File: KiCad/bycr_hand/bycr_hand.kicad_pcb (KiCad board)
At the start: 2 copper layers, 26 parts, among them J1 Conn_01x03, J2 Conn_01x03, J3 Conn_01x03, J4 Conn_01x03, J5 Conn_01x02, J6 Conn_01x02, SW1 SW_Push, U1 74HC595, U3 74HC165

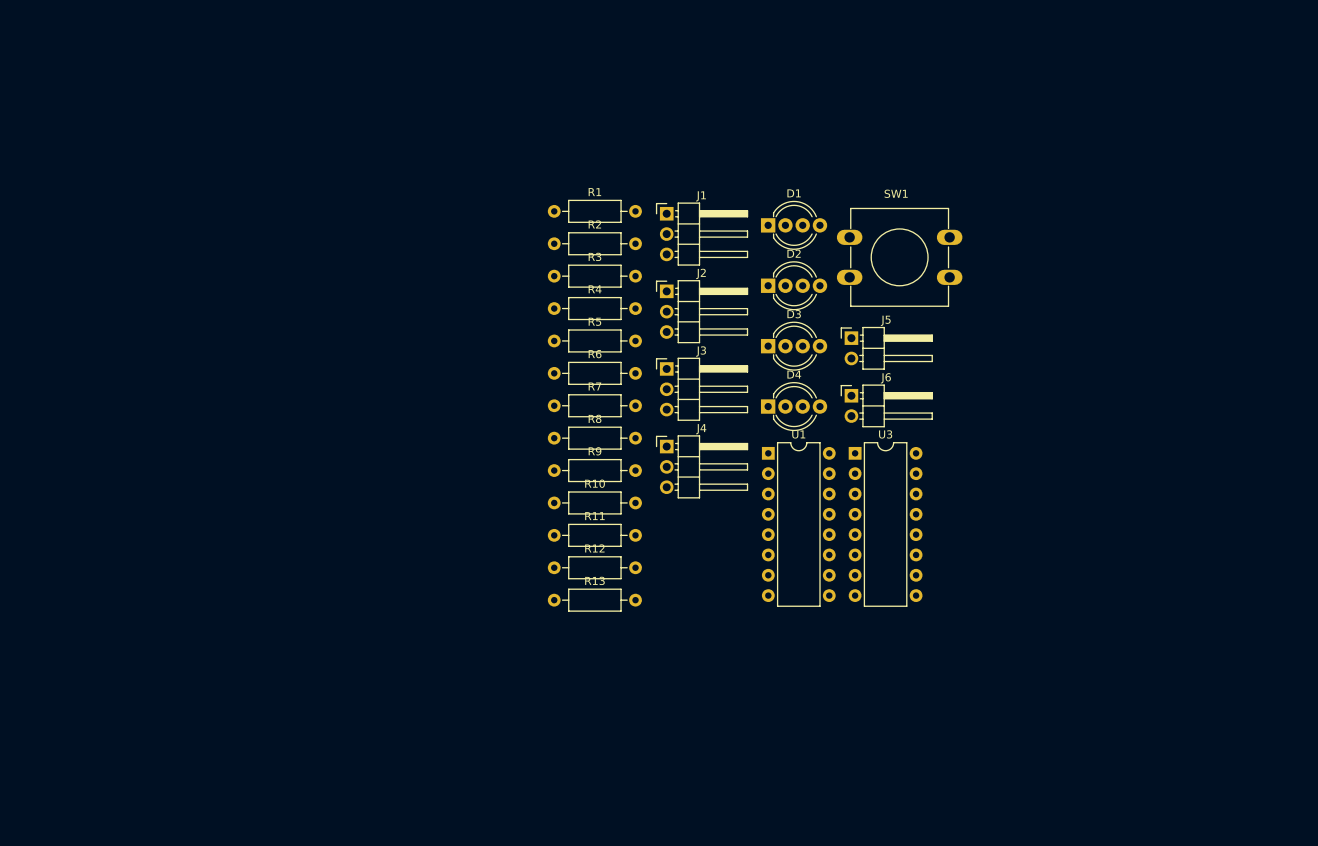
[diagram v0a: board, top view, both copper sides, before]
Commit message: rename bycr to bycr_hand
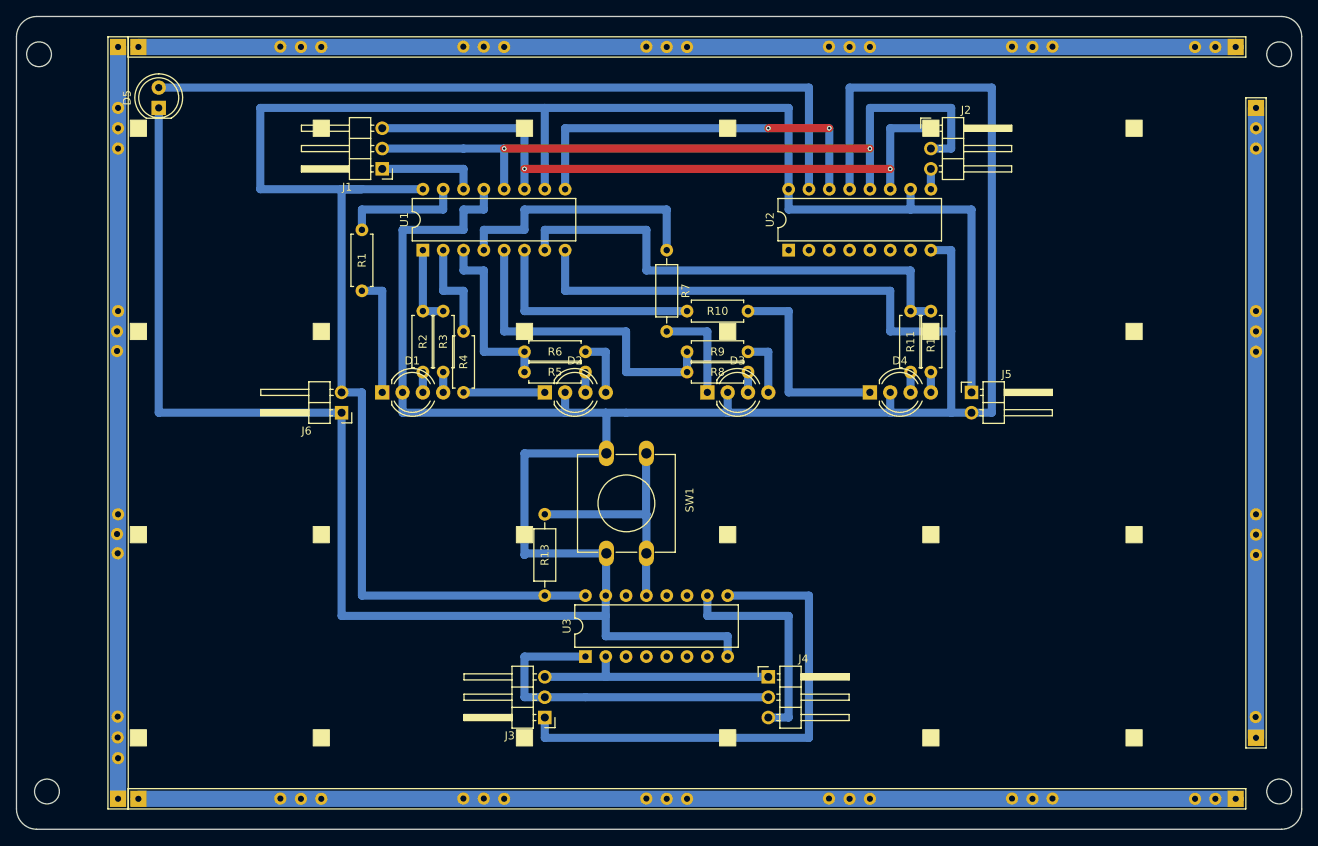
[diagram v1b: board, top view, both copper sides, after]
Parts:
- added D5: LED, LED_THT:LED_D5.0mm, F.Cu at (86.4, 58.4)
- added REF**: PCB_M, New_Library:PCB_M, F.Cu at (81.3, 50.8)
- added U2: 74HC595, Package_DIP:DIP-16_W7.62mm, F.Cu at (165.1, 76.2)
- D1, D2, D3, D4: footprint LED_THT:LED_D5.0mm-4_RGB_Wide_Pins -> Custom:LED_D5.0mm-4_RGB_Wide_Pins_Custom
- R1, R10, R11, R12, R2, R3, R4, R5, R6, R8, R9: footprint Resistor_THT:R_Axial_DIN0207_L6.3mm_D2.5mm_P10.16mm_Horizontal -> Resistor_THT:R_Axial_DIN0207_L6.3mm_D2.5mm_P7.62mm_Horizontal
- moved J6 63.8 mm to (109.2, 96.5), turned to 180 degrees
- moved R12 57.0 mm to (182.9, 83.8), turned to -90 degrees
- moved R11 52.6 mm to (180.3, 83.8), turned to -90 degrees
- moved D1 52.1 mm to (114.8, 94.0)
- moved U1 50.1 mm to (119.4, 76.2), turned to 90 degrees
- moved J3 46.2 mm to (134.6, 134.6), turned to 180 degrees
- moved U3 42.2 mm to (139.7, 127.0), turned to 90 degrees
- moved J2 38.8 mm to (182.9, 61.0)
- moved SW1 37.1 mm to (147.3, 101.6), turned to -90 degrees
- moved J1 36.0 mm to (114.3, 66.0), turned to 180 degrees
- moved J4 31.5 mm to (162.6, 129.5)
- moved D2 30.5 mm to (135.1, 94.0)
- moved R10 29.2 mm to (152.4, 83.8)
- moved R1 24.2 mm to (111.8, 73.7), turned to -90 degrees
- moved R7 24.0 mm to (149.9, 76.2), turned to -90 degrees
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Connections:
- J2 pad 1: Net-(J2-Pin_1) -> /output_clk
- J2 pad 3: /output_clk -> Net-(J2-Pin_3)
- J4 pad 1: Net-(J4-Pin_1) -> /input_clk
- J4 pad 3: /input_clk -> Net-(J4-Pin_3)
- J5 pad 1: GNDREF -> VCC
- J5 pad 2: VCC -> GNDREF
- R13 pad 2: Net-(U3-D7) -> Net-(U3-D2)
- SW1 pad 1: Net-(U3-D7) -> Net-(U3-D2)
- U1 pad 11: /output_latch -> /output_clk
- U1 pad 12: /output_clk -> /output_latch
- U1 pad 9: Net-(J2-Pin_1) -> Net-(U1-QH')
- U3 pad 10: Net-(J4-Pin_1) -> Net-(J4-Pin_3)
- U3 pad 13: unconnected-(U3-D2-Pad13) -> Net-(U3-D2)
- U3 pad 6: Net-(U3-D7) -> unconnected-(U3-D7-Pad6)
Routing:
- net GNDREF: track 0.00 -> 457.7 mm
- net VCC: track 0.00 -> 254.0 mm
- net Net-(D5-A): track 0.00 -> 94.0 mm
- net /output_latch: track 0.00 -> 94.0 mm, vias 0 -> 2
- net /output_clk: track 0.00 -> 83.8 mm, vias 0 -> 2
- net Net-(J3-Pin_1): track 0.00 -> 63.5 mm
- net Net-(U1-QH): track 0.00 -> 61.0 mm
- net Net-(U1-QH'): track 0.00 -> 48.3 mm, vias 0 -> 2
- net /input_latch: track 0.00 -> 43.2 mm
- net Net-(U1-QF): track 0.00 -> 40.6 mm
- net Net-(U1-QE): track 0.00 -> 33.0 mm
- net /input_clk: track 0.00 -> 30.5 mm
- net Net-(U3-D2): track 0.00 -> 29.2 mm
- net Net-(J4-Pin_3): track 0.00 -> 27.9 mm
- net Net-(U1-QG): track 0.00 -> 27.9 mm
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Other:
- board outline added: 160.7 x 101.6 mm

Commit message: fix bycr PCB layout
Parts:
- moved D1 2.54 mm to (112.3, 94.0)
- moved R3 2.54 mm to (119.4, 83.8)
- moved R2 2.54 mm to (116.8, 83.8)
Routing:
- net VCC: track 254.0 -> 236.2 mm
- net GNDREF: track 457.7 -> 447.5 mm
- net Net-(D1-RA): track 15.2 -> 12.7 mm
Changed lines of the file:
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@@
 	(footprint "Custom:LED_D5.0mm-4_RGB_Wide_Pins_Custom"
 		(layer "F.Cu")
-		(at 114.808 93.98)
+		(at 112.268 93.98)
 		(descr "LED, diameter 5.0mm, 4 pins, WP154A4, https://www.kingbright.com/attachments/file/psearch/000/00/00/L-154A4SUREQBFZGEW(Ver.11A).pdf")
 		(tags "LED diameter 5.0mm 2 pins diameter 5.0mm 3 pins diameter 5.0mm 4 pins RGB RGBLED")
@@
 	(footprint "Resistor_THT:R_Axial_DIN0207_L6.3mm_D2.5mm_P7.62mm_Horizontal"
 		(layer "F.Cu")
-		(at 121.92 83.82 -90)
+		(at 119.38 83.82 -90)
 		(descr "Resistor, Axial_DIN0207 series, Axial, Horizontal, pin pitch=7.62mm, 0.25W = 1/4W, length*diameter=6.3*2.5mm^2, http://cdn-reichelt.de/documents/datenblatt/B400/1_4W%23YAG.pdf")
 		(tags "Resistor Axial_DIN0207 series Axial Horizontal pin pitch 7.62mm 0.25W = 1/4W length 6.3mm diameter 2.5mm")
@@
 	(footprint "Resistor_THT:R_Axial_DIN0207_L6.3mm_D2.5mm_P7.62mm_Horizontal"
 		(layer "F.Cu")
-		(at 119.38 83.82 -90)
+		(at 116.84 83.82 -90)
 		(descr "Resistor, Axial_DIN0207 series, Axial, Horizontal, pin pitch=7.62mm, 0.25W = 1/4W, length*diameter=6.3*2.5mm^2, http://cdn-reichelt.de/documents/datenblatt/B400/1_4W%23YAG.pdf")
 		(tags "Resistor Axial_DIN0207 series Axial Horizontal pin pitch 7.62mm 0.25W = 1/4W length 6.3mm diameter 2.5mm")
@@
 	)
 	(segment
-		(start 114.3 81.28)
-		(end 114.3 93.98)
+		(start 111.76 81.28)
+		(end 111.76 93.98)
 		(width 1.016)
 		(layer "B.Cu")
@@
 	)
 	(segment
-		(start 111.76 81.28)
-		(end 114.3 81.28)
+		(start 119.38 91.44)
+		(end 119.38 93.98)
 		(width 1.016)
 		(layer "B.Cu")
-		(net 1)
+		(net 2)
 	)
 	(segment
-		(start 121.92 91.44)
-		(end 121.92 93.599)
+		(start 116.84 91.44)
+		(end 116.84 93.98)
 		(width 1.016)
 		(layer "B.Cu")
-		(net 2)
+		(net 3)
 	)
 	(segment
-		(start 121.92 93.599)
-		(end 121.539 93.98)
+		(start 114.3 93.98)
+		(end 114.3 96.52)
 		(width 1.016)
 		(layer "B.Cu")
-		(net 2)
+		(net 4)
 	)
 	(segment
-		(start 119.38 91.44)
-		(end 119.38 93.98)
+		(start 114.3 96.52)
+		(end 137.16 96.52)
 		(width 1.016)
 		(layer "B.Cu")
-		(net 3)
+		(net 4)
 	)
 	(segment
@@
 	)
 	(segment
-		(start 142.32 96.6)
-		(end 142.24 96.52)
-		(width 1.016)
-		(layer "B.Cu")
-		(net 4)
-	)
-	(segment
-		(start 109.22 96.52)
-		(end 86.36 96.52)
+		(start 127 71.12)
+		(end 127 68.58)
 		(width 1.016)
 		(layer "B.Cu")
@@
 	)
 	(segment
-		(start 124.46 73.66)
-		(end 116.84 73.66)
+		(start 142.32 96.6)
+		(end 142.24 96.52)
 		(width 1.016)
 		(layer "B.Cu")
@@
 	)
 	(segment
-		(start 116.84 96.52)
-		(end 116.84 93.98)
+		(start 124.46 71.12)
+		(end 127 71.12)
 		(width 1.016)
 		(layer "B.Cu")
@@
 	)
 	(segment
+		(start 114.3 93.98)
+		(end 114.3 73.66)
+		(width 1.016)
+		(layer "B.Cu")
+		(net 4)
+	)
+	(segment
 		(start 177.8 81.28)
 		(end 177.8 86.36)
@@
 	)
 	(segment
-		(start 190.5 96.52)
-		(end 190.5 55.88)
+		(start 83.82 53.34)
+		(end 172.72 53.34)
 		(width 1.016)
 		(layer "B.Cu")
@@
 	)
 	(segment
-		(start 187.96 96.52)
-		(end 190.5 96.52)
+		(start 190.5 96.52)
+		(end 190.5 55.88)
 		(width 1.016)
 		(layer "B.Cu")
@@
 	)
 	(segment
-		(start 116.84 73.66)
-		(end 116.84 93.98)
+		(start 187.96 96.52)
+		(end 190.5 96.52)
 		(width 1.016)
 		(layer "B.Cu")
@@
 	)
 	(segment
-		(start 124.46 71.12)
-		(end 124.46 73.66)
+		(start 124.46 73.66)
+		(end 124.46 71.12)
 		(width 1.016)
 		(layer "B.Cu")
@@
 	)
 	(segment
-		(start 127 68.58)
-		(end 127 71.12)
+		(start 114.3 96.52)
+		(end 109.22 96.52)
 		(width 1.016)
 		(layer "B.Cu")
@@
 	)
 	(segment
+		(start 172.72 53.34)
+		(end 172.72 55.88)
+		(width 1.016)
+		(layer "B.Cu")
+		(net 4)
+	)
+	(segment
+		(start 83.82 58.42)
+		(end 83.82 53.34)
+		(width 1.016)
+		(layer "B.Cu")
+		(net 4)
+	)
+	(segment
 		(start 137.16 76.2)
 		(end 137.16 81.28)
@@
 	)
 	(segment
-		(start 109.22 121.92)
-		(end 142.24 121.92)
-		(width 1.016)
-		(layer "B.Cu")
-		(net 4)
-	)
-	(segment
 		(start 185.42 76.2)
 		(end 185.42 86.36)
@@
 	)
 	(segment
+		(start 86.36 58.42)
+		(end 83.82 58.42)
+		(width 1.016)
+		(layer "B.Cu")
+		(net 4)
+	)
+	(segment
 		(start 177.8 86.36)
 		(end 185.42 86.36)
@@
 	)
 	(segment
-		(start 109.22 96.52)
-		(end 109.22 121.92)
+		(start 114.3 73.66)
+		(end 124.46 73.66)
 		(width 1.016)
 		(layer "B.Cu")
@@
 	)
 	(segment
-		(start 127 71.12)
-		(end 124.46 71.12)
-		(width 1.016)
-		(layer "B.Cu")
-		(net 4)
-	)
-	(segment
-		(start 116.84 96.52)
-		(end 137.16 96.52)
-		(width 1.016)
-		(layer "B.Cu")
-		(net 4)
-	)
-	(segment
-		(start 86.36 96.52)
-		(end 86.36 58.42)
-		(width 1.016)
-		(layer "B.Cu")
-		(net 4)
-	)
-	(segment
 		(start 177.8 96.52)
 		(end 185.42 96.52)
@@
 	)
 	(segment
-		(start 165.1 93.98)
-		(end 165.1 83.82)
-		(width 1.016)
-		(layer "B.Cu")
-		(net 11)
-	)
-	(segment
 		(start 175.26 93.98)
-		(end 165.1 93.98)
+		(end 175.26 83.82)
 		(width 1.016)
 		(layer "B.Cu")
@@
 	)
 	(segment
-		(start 165.1 83.82)
+		(start 175.26 83.82)
 		(end 160.02 83.82)
 		(width 1.016)
@@
 	)
 	(segment
-		(start 111.76 93.98)
-		(end 109.22 93.98)
-		(width 1.016)
-		(layer "B.Cu")
-		(net 19)
-	)
-	(segment
 		(start 165.1 68.58)
 		(end 165.1 71.12)
@@
 	)
 	(segment
-		(start 99.06 58.42)
-		(end 99.06 68.58)
-		(width 1.016)
-		(layer "B.Cu")
-		(net 19)
-	)
-	(segment
 		(start 187.96 71.12)
 		(end 187.96 93.98)
@@
 	(segment
 		(start 134.62 58.42)
-		(end 99.06 58.42)
+		(end 109.22 58.42)
 		(width 1.016)
 		(layer "B.Cu")
@@
 	)
 	(segment
-		(start 111.76 119.38)
-		(end 111.76 93.98)
+		(start 106.68 119.38)
+		(end 134.62 119.38)
 		(width 1.016)
 		(layer "B.Cu")
@@
 	)
 	(segment
-		(start 165.1 71.12)
-		(end 180.34 71.12)
+		(start 109.22 93.98)
+		(end 106.68 93.98)
 		(width 1.016)
 		(layer "B.Cu")
@@
 	)
 	(segment
-		(start 134.62 119.38)
-		(end 111.76 119.38)
+		(start 165.1 71.12)
+		(end 180.34 71.12)
 		(width 1.016)
 		(layer "B.Cu")
@@
 	)
 	(segment
-		(start 99.06 68.58)
-		(end 111.76 68.58)
-		(width 1.016)
-		(layer "B.Cu")
-		(net 19)
-	)
-	(segment
 		(start 109.22 68.58)
 		(end 109.22 93.98)
@@
 	)
 	(segment
+		(start 109.22 68.58)
+		(end 109.22 58.42)
+		(width 1.016)
+		(layer "B.Cu")
+		(net 19)
+	)
+	(segment
 		(start 111.76 68.58)
 		(end 109.22 68.58)
@@
 	)
 	(segment
+		(start 106.68 93.98)
+		(end 106.68 119.38)
+		(width 1.016)
+		(layer "B.Cu")
+		(net 19)
+	)
+	(segment
 		(start 121.92 71.12)
 		(end 121.92 68.58)
@@
 	)
 	(segment
-		(start 119.38 83.82)
-		(end 121.92 83.82)
-		(width 1.016)
-		(layer "B.Cu")
-		(net 21)
-	)
-	(segment
 		(start 119.38 76.2)
 		(end 119.38 83.82)
@@
 	)
 	(segment
-		(start 124.46 81.28)
-		(end 124.46 86.36)
+		(start 119.38 83.82)
+		(end 116.84 83.82)
 		(width 1.016)
 		(layer "B.Cu")
-		(net 22)
+		(net 21)
 	)
 	(segment
-		(start 121.92 76.2)
-		(end 121.92 81.28)
+		(start 124.46 86.36)
+		(end 121.92 86.36)
 		(width 1.016)
 		(layer "B.Cu")
@@
 	)
 	(segment
-		(start 121.92 81.28)
-		(end 124.46 81.28)
+		(start 121.92 86.36)
+		(end 121.92 76.2)
 		(width 1.016)
 		(layer "B.Cu")
@@
 	)
 	(segment
-		(start 124.46 76.2)
-		(end 124.46 78.74)
+		(start 127 88.9)
+		(end 132.08 88.9)
 		(width 1.016)
 		(layer "B.Cu")
@@
 	)
 	(segment
-		(start 127 88.9)
-		(end 132.08 88.9)
+		(start 127 83.82)
+		(end 127 88.9)
 		(width 1.016)
 		(layer "B.Cu")
@@
 	)
 	(segment
-		(start 127 78.74)
-		(end 127 88.9)
+		(start 124.46 76.2)
+		(end 124.46 83.82)
 		(width 1.016)
 		(layer "B.Cu")
@@
 	)
 	(segment
-		(start 124.46 78.74)
-		(end 127 78.74)
+		(start 124.46 83.82)
+		(end 127 83.82)
 		(width 1.016)
 		(layer "B.Cu")

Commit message: fix bycr_hand PCB layout
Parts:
- moved D1 2.54 mm to (114.8, 94.0)
- moved R3 2.54 mm to (121.9, 83.8)
- moved R2 2.54 mm to (119.4, 83.8)
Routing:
- net GNDREF: track 447.5 -> 424.7 mm
- net Net-(U1-QF): track 40.6 -> 38.1 mm
- net Net-(D1-RA): track 12.7 -> 15.2 mm
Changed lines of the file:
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@@
 	(footprint "Custom:LED_D5.0mm-4_RGB_Wide_Pins_Custom"
 		(layer "F.Cu")
-		(at 112.268 93.98)
+		(at 114.808 93.98)
 		(descr "LED, diameter 5.0mm, 4 pins, WP154A4, https://www.kingbright.com/attachments/file/psearch/000/00/00/L-154A4SUREQBFZGEW(Ver.11A).pdf")
 		(tags "LED diameter 5.0mm 2 pins diameter 5.0mm 3 pins diameter 5.0mm 4 pins RGB RGBLED")
@@
 	(footprint "Resistor_THT:R_Axial_DIN0207_L6.3mm_D2.5mm_P7.62mm_Horizontal"
 		(layer "F.Cu")
-		(at 119.38 83.82 -90)
+		(at 121.92 83.82 -90)
 		(descr "Resistor, Axial_DIN0207 series, Axial, Horizontal, pin pitch=7.62mm, 0.25W = 1/4W, length*diameter=6.3*2.5mm^2, http://cdn-reichelt.de/documents/datenblatt/B400/1_4W%23YAG.pdf")
 		(tags "Resistor Axial_DIN0207 series Axial Horizontal pin pitch 7.62mm 0.25W = 1/4W length 6.3mm diameter 2.5mm")
@@
 	(footprint "Resistor_THT:R_Axial_DIN0207_L6.3mm_D2.5mm_P7.62mm_Horizontal"
 		(layer "F.Cu")
-		(at 116.84 83.82 -90)
+		(at 119.38 83.82 -90)
 		(descr "Resistor, Axial_DIN0207 series, Axial, Horizontal, pin pitch=7.62mm, 0.25W = 1/4W, length*diameter=6.3*2.5mm^2, http://cdn-reichelt.de/documents/datenblatt/B400/1_4W%23YAG.pdf")
 		(tags "Resistor Axial_DIN0207 series Axial Horizontal pin pitch 7.62mm 0.25W = 1/4W length 6.3mm diameter 2.5mm")
@@
 	)
 	(segment
-		(start 111.76 81.28)
-		(end 111.76 93.98)
+		(start 111.76 93.98)
+		(end 114.3 93.98)
 		(width 1.016)
 		(layer "B.Cu")
@@
 	)
 	(segment
-		(start 119.38 91.44)
-		(end 119.38 93.98)
-		(width 1.016)
-		(layer "B.Cu")
-		(net 2)
-	)
-	(segment
-		(start 116.84 91.44)
-		(end 116.84 93.98)
+		(start 111.76 81.28)
+		(end 111.76 93.98)
 		(width 1.016)
 		(layer "B.Cu")
-		(net 3)
+		(net 1)
 	)
 	(segment
-		(start 114.3 93.98)
-		(end 114.3 96.52)
+		(start 121.92 91.44)
+		(end 121.92 93.98)
 		(width 1.016)
 		(layer "B.Cu")
-		(net 4)
+		(net 2)
 	)
 	(segment
-		(start 114.3 96.52)
-		(end 137.16 96.52)
+		(start 119.38 91.44)
+		(end 119.38 93.98)
 		(width 1.016)
 		(layer "B.Cu")
-		(net 4)
+		(net 3)
 	)
 	(segment
@@
 	)
 	(segment
-		(start 114.3 93.98)
-		(end 114.3 73.66)
-		(width 1.016)
-		(layer "B.Cu")
-		(net 4)
-	)
-	(segment
-		(start 177.8 81.28)
-		(end 177.8 86.36)
-		(width 1.016)
-		(layer "B.Cu")
-		(net 4)
-	)
-	(segment
 		(start 142.32 114.1)
 		(end 142.28 114.14)
@@
 	)
 	(segment
-		(start 137.16 81.28)
-		(end 177.8 81.28)
-		(width 1.016)
-		(layer "B.Cu")
-		(net 4)
-	)
-	(segment
 		(start 83.82 53.34)
 		(end 172.72 53.34)
@@
 	)
 	(segment
+		(start 116.84 96.52)
+		(end 137.16 96.52)
+		(width 1.016)
+		(layer "B.Cu")
+		(net 4)
+	)
+	(segment
 		(start 132.08 101.6)
 		(end 142.32 101.6)
@@
 	)
 	(segment
+		(start 116.84 93.98)
+		(end 116.84 96.52)
+		(width 1.016)
+		(layer "B.Cu")
+		(net 4)
+	)
+	(segment
+		(start 116.84 93.98)
+		(end 116.84 73.66)
+		(width 1.016)
+		(layer "B.Cu")
+		(net 4)
+	)
+	(segment
 		(start 132.08 114.3)
 		(end 132.08 101.6)
@@
 	)
 	(segment
-		(start 177.8 86.36)
-		(end 185.42 86.36)
+		(start 142.24 121.92)
+		(end 142.24 124.46)
 		(width 1.016)
 		(layer "B.Cu")
@@
 	)
 	(segment
-		(start 142.24 121.92)
-		(end 142.24 124.46)
+		(start 116.84 73.66)
+		(end 124.46 73.66)
 		(width 1.016)
 		(layer "B.Cu")
@@
 	)
 	(segment
-		(start 114.3 73.66)
-		(end 124.46 73.66)
+		(start 157.48 81.28)
+		(end 157.48 93.98)
+		(width 1.016)
+		(layer "B.Cu")
+		(net 4)
+	)
+	(segment
+		(start 137.16 81.28)
+		(end 157.48 81.28)
+		(width 1.016)
+		(layer "B.Cu")
+		(net 4)
+	)
+	(segment
+		(start 114.3 96.52)
+		(end 116.84 96.52)
 		(width 1.016)
 		(layer "B.Cu")
@@
 	(segment
 		(start 119.38 83.82)
-		(end 116.84 83.82)
+		(end 121.92 83.82)
 		(width 1.016)
 		(layer "B.Cu")
@@
 	)
 	(segment
-		(start 124.46 86.36)
-		(end 121.92 86.36)
+		(start 121.92 76.2)
+		(end 121.92 81.28)
 		(width 1.016)
 		(layer "B.Cu")
@@
 	)
 	(segment
-		(start 121.92 86.36)
-		(end 121.92 76.2)
+		(start 124.46 81.28)
+		(end 124.46 86.36)
+		(width 1.016)
+		(layer "B.Cu")
+		(net 22)
+	)
+	(segment
+		(start 121.92 81.28)
+		(end 124.46 81.28)
 		(width 1.016)
 		(layer "B.Cu")
@@
 	)
 	(segment
-		(start 127 88.9)
-		(end 132.08 88.9)
+		(start 124.46 78.74)
+		(end 127 78.74)
 		(width 1.016)
 		(layer "B.Cu")
@@
 	)
 	(segment
-		(start 127 83.82)
+		(start 127 78.74)
 		(end 127 88.9)
 		(width 1.016)
@@
 	)
 	(segment
-		(start 124.46 76.2)
-		(end 124.46 83.82)
+		(start 127 88.9)
+		(end 132.08 88.9)
 		(width 1.016)
 		(layer "B.Cu")
@@
 	)
 	(segment
-		(start 124.46 83.82)
-		(end 127 83.82)
+		(start 124.46 76.2)
+		(end 124.46 78.74)
 		(width 1.016)
 		(layer "B.Cu")
@@
 	)
 	(segment
-		(start 144.78 91.44)
-		(end 152.4 91.44)
+		(start 152.4 88.9)
+		(end 144.78 88.9)
 		(width 1.016)
 		(layer "B.Cu")
@@
 	)
 	(segment
-		(start 144.78 86.36)
-		(end 144.78 91.44)
+		(start 144.78 88.9)
+		(end 144.78 86.36)
 		(width 1.016)
 		(layer "B.Cu")
